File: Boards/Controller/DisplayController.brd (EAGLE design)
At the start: 52.9 x 39 mm, 46 parts, among them J1 USB0001LF, J100 38K8067, J3 AVR_SPI_PRG_62X3_LOCK, Q1 BSS138, U1 MCP1703CB, U100 MCP73831, U101 MAX1797, U2 FT232RQ, U3 ATMEGA328P-MU, U5 MAX1704X, X2 CRYSTAL7A-20.000MAAJ-T

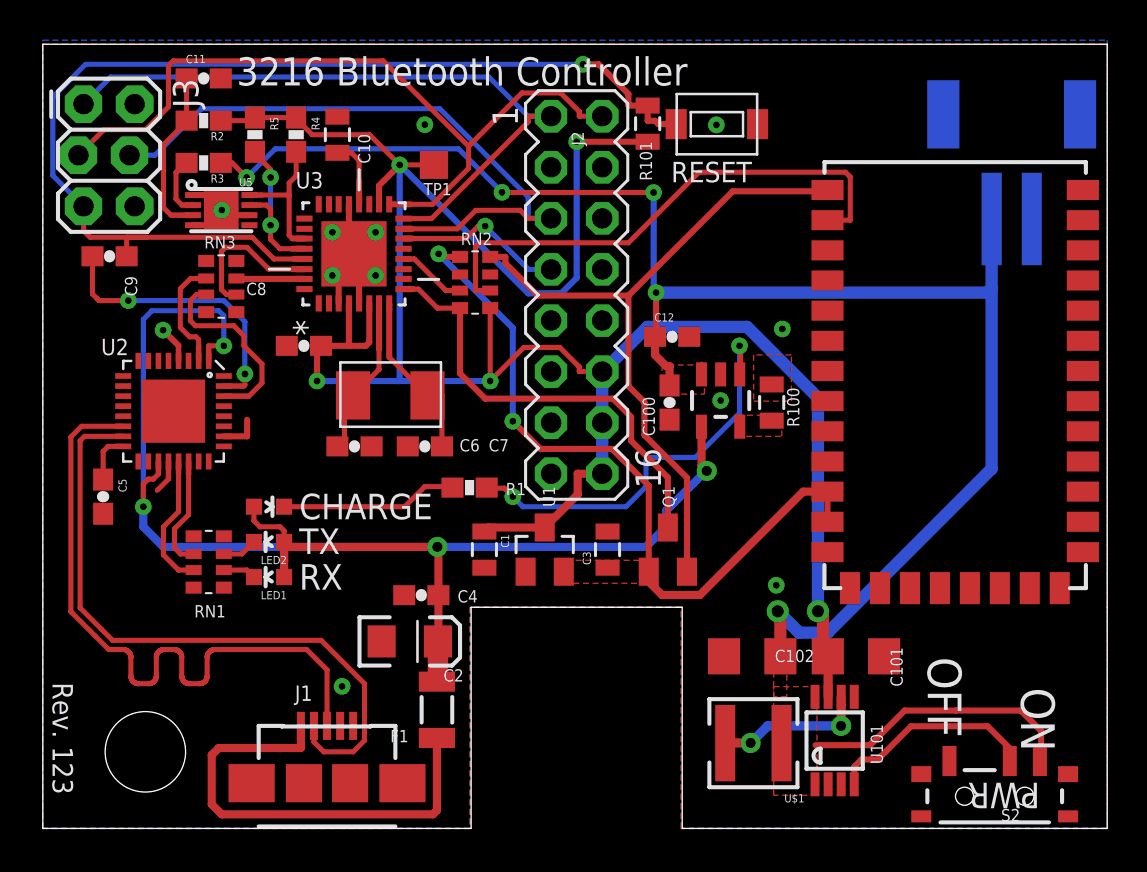
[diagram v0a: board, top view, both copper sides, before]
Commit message: Fixed bottom ground plane being .2mm above outline Cleaned up traces a bit Added 100uF cap to top power pin of atmega328p (all power pins now have a cap) Added 10k resistor to BT module reset line (to hold it high)
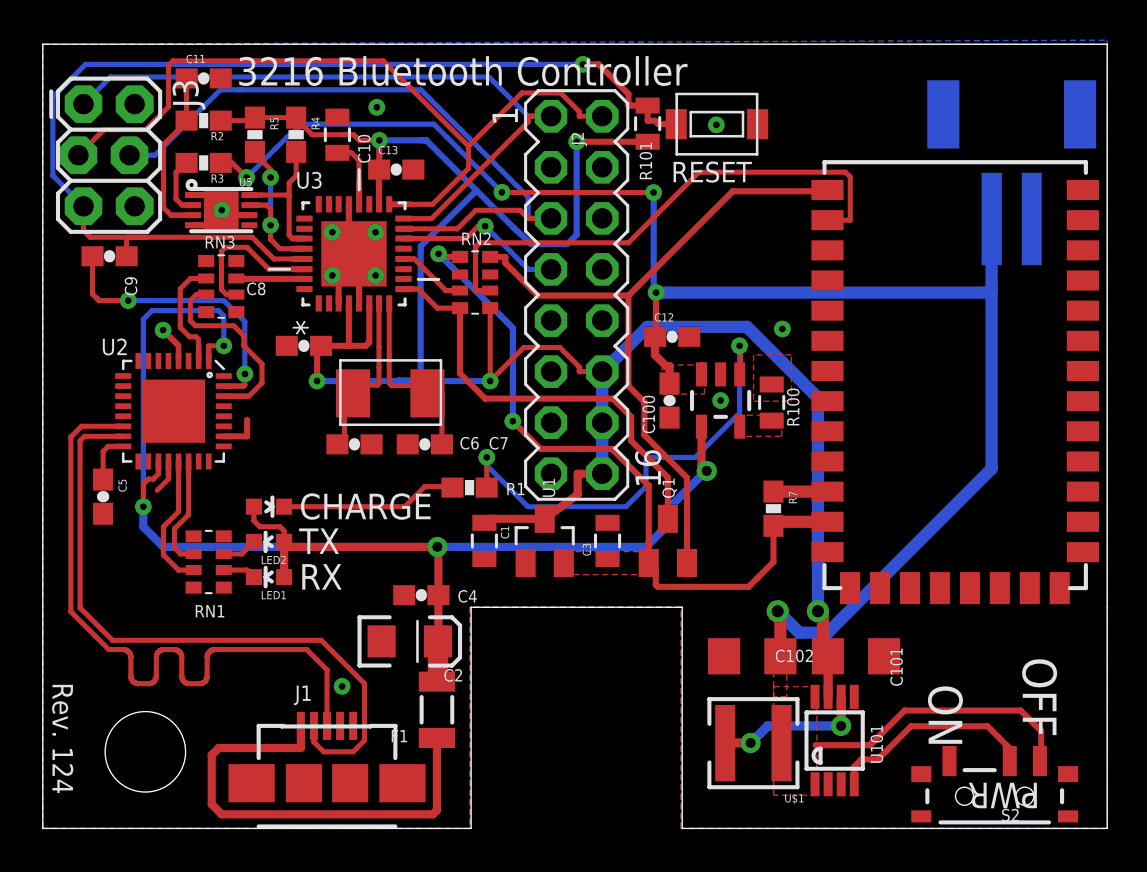
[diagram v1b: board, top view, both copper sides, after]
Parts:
- removed TP1: TPSQTP14SQ, testpad:TP14SQ
- added C13: 100nF, SparkFun:0603-CAP
- added R7: 10k, SparkFun:0603-RES
- moved C1 0.43 mm to (22.0, 14.3)
- moved C3 0.43 mm to (28.1, 14.3)
- moved Q1 0.43 mm to (31.1, 14.3)
- moved U1 0.43 mm to (25.0, 14.3)
- moved C6 0.10 mm to (15.5, 19.1)
- moved C7 0.10 mm to (19.0, 19.1)
- moved X2 0.10 mm to (17.3, 21.7)
- moved C100 0.10 mm to (31.2, 21.3)
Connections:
- new net BTRESET: R7.1, U$2.P$11
- net +3V3: now also R7.2; no longer U$2.P$11
- net GND: now also C13.2
- net VCC: now also C13.1; no longer TP1.TP
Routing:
- net VCC: track 116.2 -> 113.1 mm
- net BTRESET: track 0.00 -> 2.69 mm
- net N$5: track 20.9 -> 23.2 mm
- net +3V3: track 36.1 -> 35.1 mm
- net PACK+: track 94.5 -> 95.4 mm
- net MOSI: track 32.7 -> 33.5 mm
- net N$9: track 9.60 -> 10.3 mm
- net N$8: track 8.80 -> 9.47 mm
- net GND: vias 12 -> 11
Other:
- board text added: "Rev. 124"
- board text removed: "Rev. 123"

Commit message: connected bluetooth reset to microcontroller
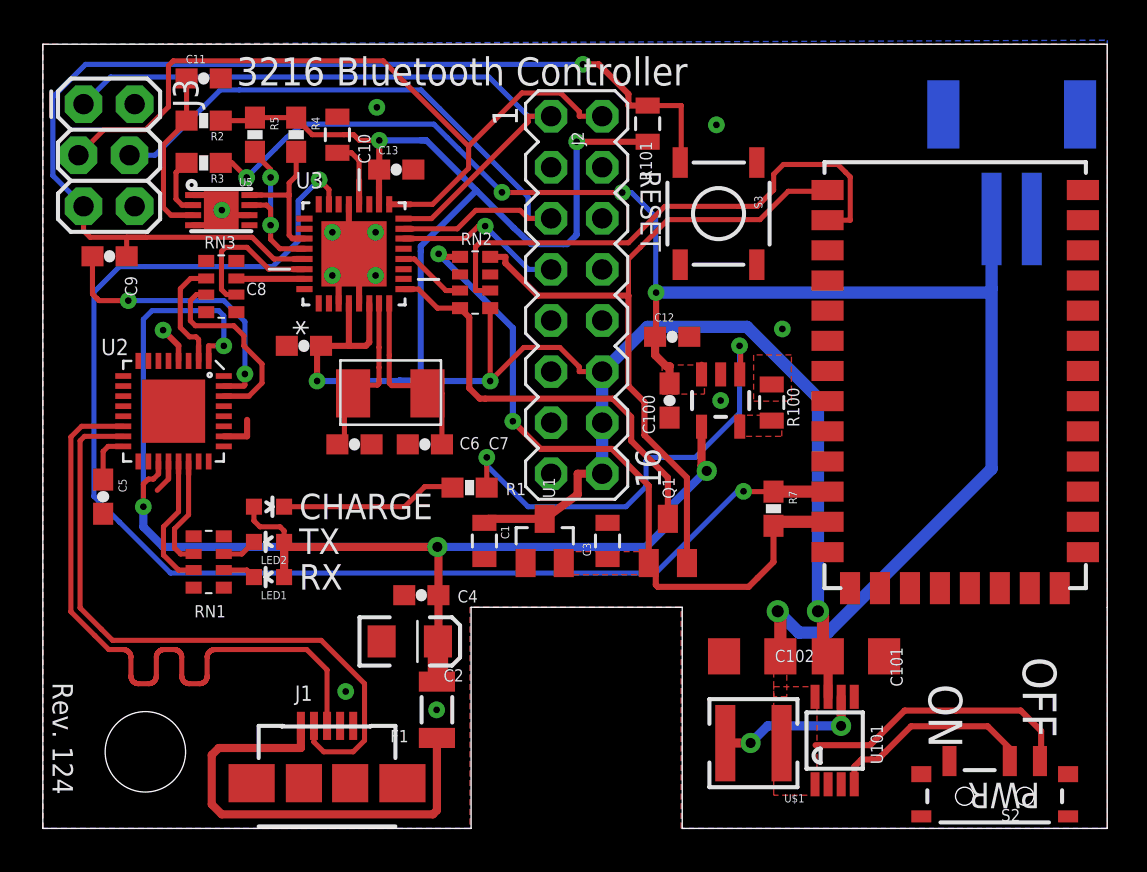
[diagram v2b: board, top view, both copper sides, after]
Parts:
- removed S1: TL1015AF160QG, MyParts:TL105
- added S3: SWITCH-MOMENTARY-2SMD, SparkFun:TACTILE_SWITCH_SMD
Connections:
- net BTRESET: now also U3.23
- net GND: now also S3.1; no longer S1.P$1
- net RESET: now also S3.3; no longer S1.P$2
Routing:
- net BTRESET: track 2.69 -> 66.0 mm, vias 0 -> 2
- net RESET: track 54.8 -> 57.3 mm
- net 3V3TX: track 34.5 -> 35.6 mm
- net 3V3RX: track 26.5 -> 27.2 mm
- net GND: vias 11 -> 12

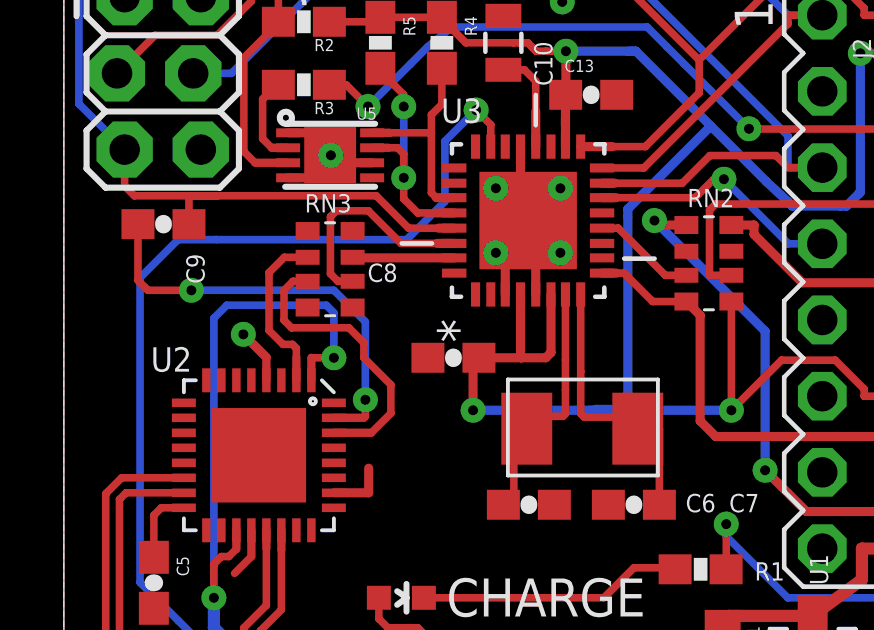
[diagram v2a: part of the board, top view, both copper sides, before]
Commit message: removed 1K resistor from TX + RX between ATMega328p and FT232RQ, not needed as nothing else is connected to these pins.
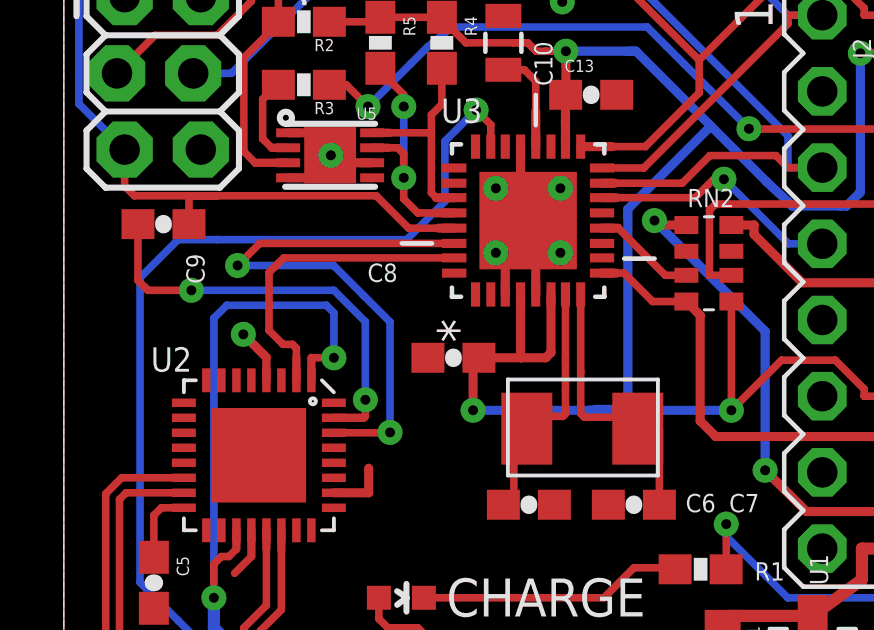
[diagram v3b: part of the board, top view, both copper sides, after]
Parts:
- removed RN3: 1k, resistor-dil:EXB38V
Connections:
- removed net N$13: RN3.3, U3.31
- removed net N$15: RN3.2, U3.30
- net RX: now also U3.30; no longer RN3.7
- net TX: now also U3.31; no longer RN3.6
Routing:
- net RX: track 9.78 -> 19.2 mm, vias 0 -> 2
- net N$15: track 7.40 -> 0.00 mm
- net TX: track 5.65 -> 10.5 mm
- net N$13: track 3.39 -> 0.00 mm
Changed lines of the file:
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@@
 <attribute name="VALUE" x="7.77" y="22.655" size="0.4318" layer="27" rot="R180"/>
-</element>
-<element name="RN3" library="resistor-dil" package="EXB38V" value="1k" x="8.875" y="26.95" smashed="yes" rot="R90">
-<attribute name="OC_NEWARK" value="15M6870" x="8.875" y="26.95" size="0.3048" layer="27" rot="R90" display="off"/>
-<attribute name="MPN" value="" x="8.875" y="26.95" size="0.3048" layer="27" rot="R90" display="off"/>
-<attribute name="MF" value="" x="8.875" y="26.95" size="0.3048" layer="27" rot="R90" display="off"/>
-<attribute name="OC_FARNELL" value="unknown" x="8.875" y="26.95" size="0.3048" layer="27" rot="R90" display="off"/>
-<attribute name="NAME" x="8.0275" y="28.845" size="0.6096" layer="25"/>
-<attribute name="VALUE" x="11.415" y="24.9775" size="1.27" layer="27" rot="R90"/>
 </element>
 <element name="J1" library="MyParts" package="10104110-0001LF" value="USB0001LF" x="14.135" y="2.25">
@@
 <wire x1="20.75" y1="26.75" x2="20.0482" y2="26.75" width="0.254" layer="1"/>
 <wire x1="20.0482" y1="26.75" x2="18.4772" y2="28.321" width="0.254" layer="1"/>
-<wire x1="18.4772" y1="28.321" x2="17.9388" y2="28.321" width="0.254" layer="1"/>
+<wire x1="18.4772" y1="28.321" x2="17.9388" y2="28.321" width="0.3048" layer="1"/>
 </signal>
 <signal name="D9">
@@
 <signal name="RX">
 <contactref element="U2" pad="30"/>
-<contactref element="RN3" pad="7"/>
-<wire x1="8.125" y1="26.55" x2="7.6382" y2="26.55" width="0.254" layer="1"/>
-<wire x1="7.6382" y1="26.55" x2="7.3382" y2="26.25" width="0.254" layer="1"/>
-<wire x1="7.3382" y1="26.25" x2="7.3382" y2="25.25" width="0.254" layer="1"/>
-<wire x1="7.3382" y1="25.25" x2="7.5882" y2="25" width="0.254" layer="1"/>
-<wire x1="7.5882" y1="25" x2="9.5" y2="25" width="0.254" layer="1"/>
-<wire x1="9.5" y1="25" x2="10" y2="24.5" width="0.254" layer="1"/>
-<wire x1="10" y1="24.5" x2="10" y2="24" width="0.254" layer="1"/>
-<wire x1="10" y1="24" x2="10.9" y2="23.1" width="0.254" layer="1"/>
-<wire x1="10.9" y1="23.1" x2="10.9" y2="22.15" width="0.254" layer="1"/>
-<wire x1="10.9" y1="22.15" x2="10.25" y2="21.5" width="0.254" layer="1"/>
-<wire x1="10.25" y1="21.5" x2="9" y2="21.5" width="0.2794" layer="1"/>
+<contactref element="U3" pad="30"/>
+<wire x1="13.0112" y1="27.813" x2="6.5278" y2="27.813" width="0.254" layer="1"/>
+<wire x1="6.5278" y1="27.813" x2="5.7912" y2="27.0764" width="0.254" layer="1"/>
+<via x="5.7912" y="27.0764" extent="1-16" drill="0.3302"/>
+<wire x1="5.7912" y1="27.0764" x2="8.9916" y2="27.0764" width="0.254" layer="16"/>
+<wire x1="8.9916" y1="27.0764" x2="10.0076" y2="26.0604" width="0.254" layer="16"/>
+<wire x1="10.0076" y1="26.0604" x2="10.8712" y2="25.1968" width="0.254" layer="16"/>
+<wire x1="10.8712" y1="25.1968" x2="10.8712" y2="21.5138" width="0.254" layer="16"/>
+<via x="10.8712" y="21.5138" extent="1-16" drill="0.3302"/>
+<wire x1="10.8712" y1="21.5138" x2="10.6426" y2="21.5138" width="0.254" layer="1"/>
+<wire x1="10.6426" y1="21.5138" x2="10.6426" y2="21.5392" width="0.254" layer="1"/>
+<wire x1="9" y1="21.5" x2="10.8712" y2="21.5" width="0.254" layer="1"/>
+<wire x1="10.8712" y1="21.5" x2="10.8712" y2="21.5138" width="0.254" layer="1"/>
 </signal>
 <signal name="TX">
 <contactref element="U2" pad="2"/>
-<contactref element="RN3" pad="6"/>
 <wire x1="7.75" y1="24" x2="7.75" y2="24.3175" width="0.254" layer="1"/>
 <wire x1="7.75" y1="24.3175" x2="7.62" y2="24.4475" width="0.254" layer="1"/>
@@
 <wire x1="7.3025" y1="24.4475" x2="6.8382" y2="24.9118" width="0.254" layer="1"/>
 <wire x1="6.8382" y1="24.9118" x2="6.8382" y2="26.8407" width="0.254" layer="1"/>
-<wire x1="6.8382" y1="26.8407" x2="7.3475" y2="27.35" width="0.254" layer="1"/>
-<wire x1="7.3475" y1="27.35" x2="8.125" y2="27.35" width="0.254" layer="1"/>
+<wire x1="6.8382" y1="26.8407" x2="7.14375" y2="27.14625" width="0.254" layer="1"/>
 <wire x1="7.75" y1="23.25" x2="7.75" y2="24" width="0.2794" layer="1"/>
-</signal>
-<signal name="N$13">
 <contactref element="U3" pad="31"/>
-<contactref element="RN3" pad="3"/>
-<wire x1="9.625" y1="27.35" x2="9.6446" y2="27.3304" width="0.3048" layer="1"/>
-<wire x1="9.6446" y1="27.3304" x2="13.0112" y2="27.3304" width="0.3048" layer="1"/>
-</signal>
-<signal name="N$15">
-<contactref element="U3" pad="30"/>
-<contactref element="RN3" pad="2"/>
-<wire x1="9.625" y1="26.55" x2="9.135" y2="26.55" width="0.254" layer="1"/>
-<wire x1="9.135" y1="26.55" x2="8.885" y2="26.8" width="0.254" layer="1"/>
-<wire x1="8.885" y1="26.8" x2="8.885" y2="28.7" width="0.254" layer="1"/>
-<wire x1="8.885" y1="28.7" x2="9.085" y2="28.9" width="0.254" layer="1"/>
-<wire x1="9.085" y1="28.9" x2="10.15" y2="28.9" width="0.254" layer="1"/>
-<wire x1="10.15" y1="28.9" x2="11.237" y2="27.813" width="0.254" layer="1"/>
-<wire x1="11.237" y1="27.813" x2="12.437" y2="27.813" width="0.254" layer="1"/>
-<wire x1="12.437" y1="27.813" x2="13.0112" y2="27.813" width="0.3048" layer="1"/>
+<wire x1="13.0112" y1="27.3304" x2="7.3279" y2="27.3304" width="0.254" layer="1"/>
+<wire x1="7.3279" y1="27.3304" x2="7.14375" y2="27.14625" width="0.254" layer="1"/>
 </signal>
 <signal name="N$16">
@@
 <wire x1="1.8536" y1="10.9697" x2="2.9116" y2="9.9116" width="0.254" layer="1"/>
 <wire x1="2.9116" y1="9.9116" x2="3.4697" y2="9.3536" width="0.254" layer="1"/>
-<wire x1="3.4697" y1="9.3536" x2="13.8464" y2="9.3536" width="0.254" layer="1"/>
 <wire x1="13.8464" y1="9.3536" x2="16" y2="7.2" width="0.254" layer="1"/>
 <wire x1="16" y1="7.2" x2="16" y2="4.375" width="0.254" layer="1"/>
@@
 <wire x1="13.97" y1="3.81" x2="13.485" y2="4.295" width="0.254" layer="1"/>
 <wire x1="13.485" y1="4.295" x2="13.485" y2="5.1" width="0.254" layer="1"/>
+<wire x1="3.4697" y1="9.3536" x2="13.8464" y2="9.3536" width="0.254" layer="1"/>
 </signal>
 <signal name="USB_P">

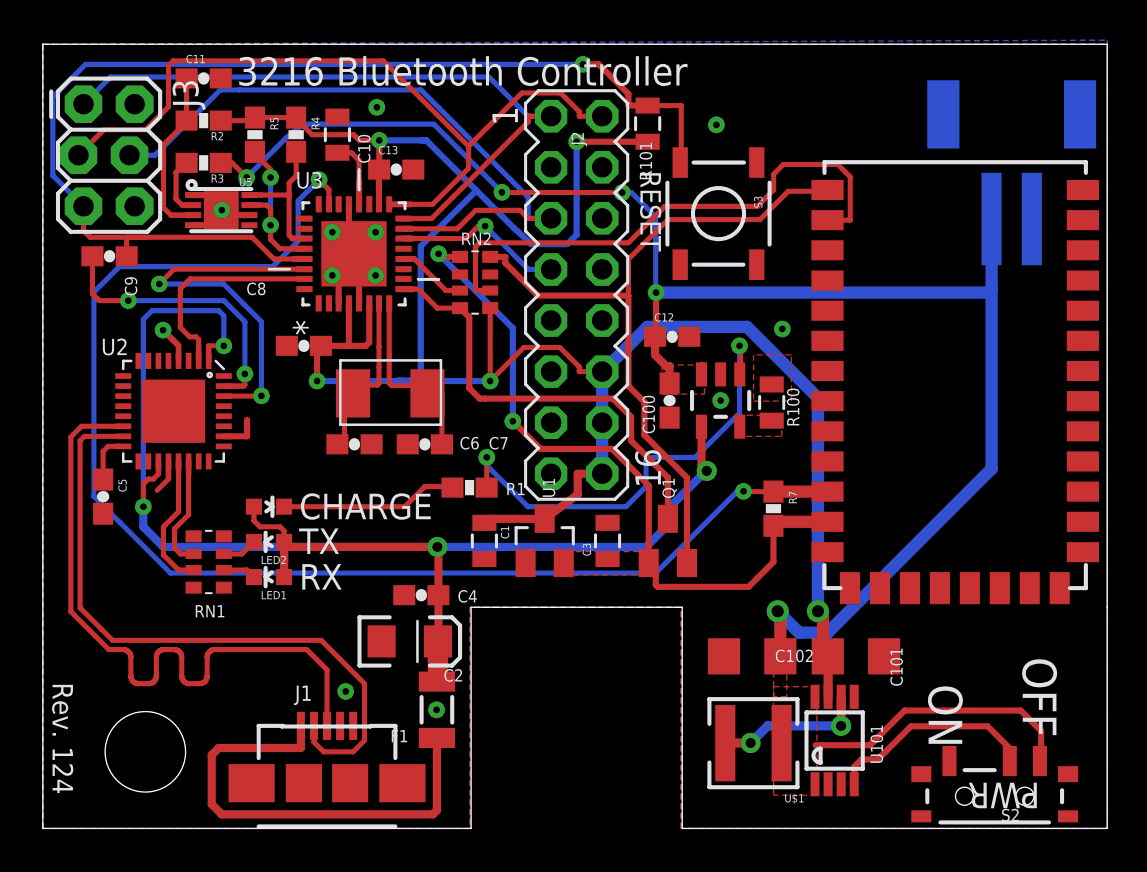
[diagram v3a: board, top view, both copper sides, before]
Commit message: Added Switching diode to reset line on atmega328 (per arduino forums/Uno R3 design)
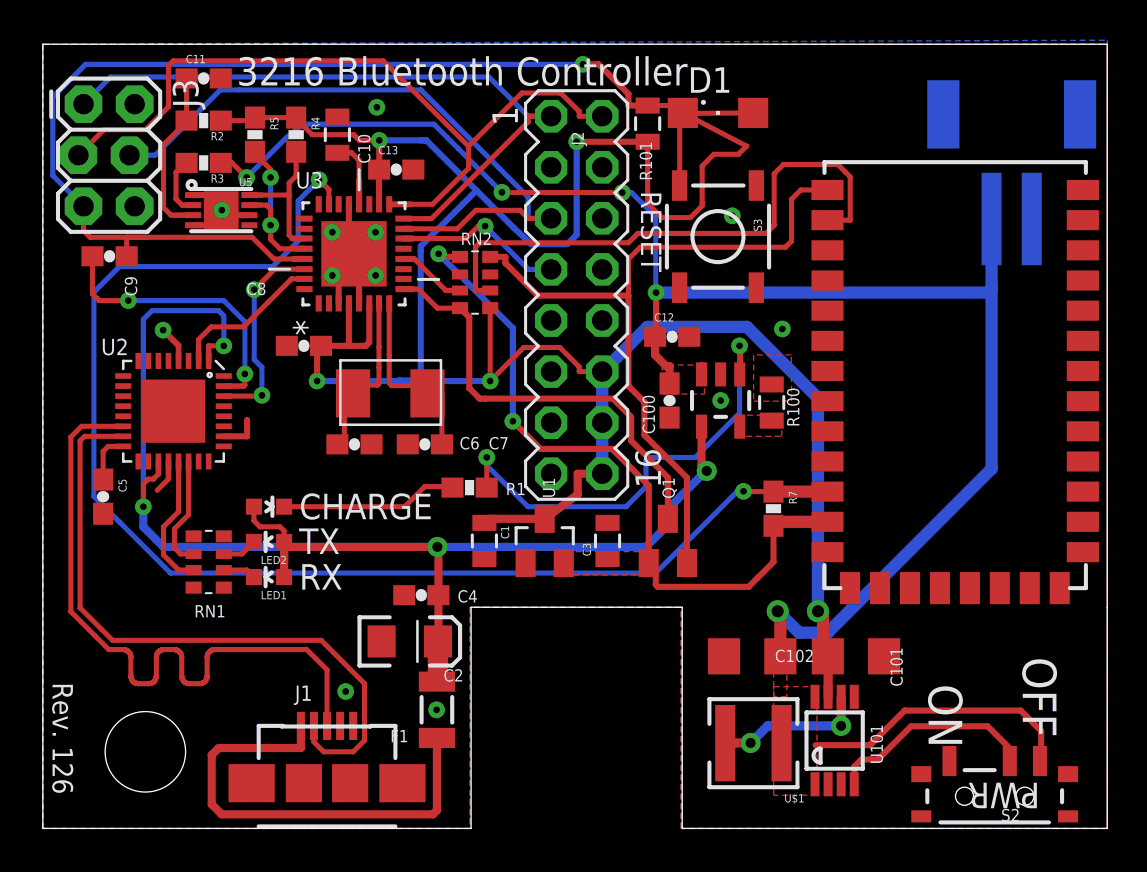
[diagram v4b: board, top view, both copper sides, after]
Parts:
- added D1: (no value), MyParts:SML1206
- moved S3 1.14 mm to (33.6, 29.4)
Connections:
- net RESET: now also D1.A
- net VCC: now also D1.C
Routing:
- net VCC: track 113.1 -> 127.6 mm
- net RX: track 19.2 -> 10.2 mm
- net RESET: track 57.3 -> 62.1 mm
- net TX: track 10.5 -> 7.58 mm
- net 3V3TX: track 35.6 -> 36.8 mm
- net 3V3RX: track 27.2 -> 28.3 mm
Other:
- board text added: "Rev. 126"
- board text removed: "Rev. 124"
